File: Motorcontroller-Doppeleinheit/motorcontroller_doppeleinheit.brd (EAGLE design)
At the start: 75 x 65 mm, 24 parts, among them Q1 16,384Mhz

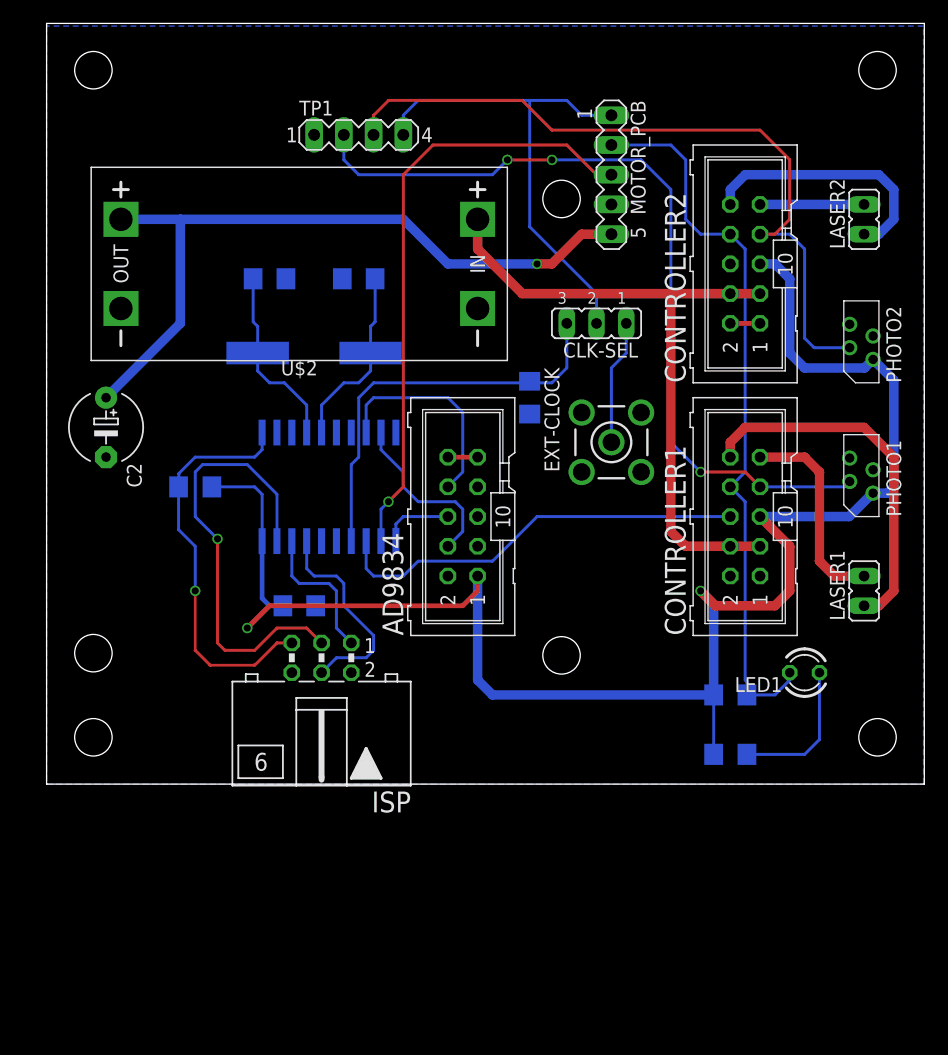
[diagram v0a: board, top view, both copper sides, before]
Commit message: Added R4 for current limit if powering on
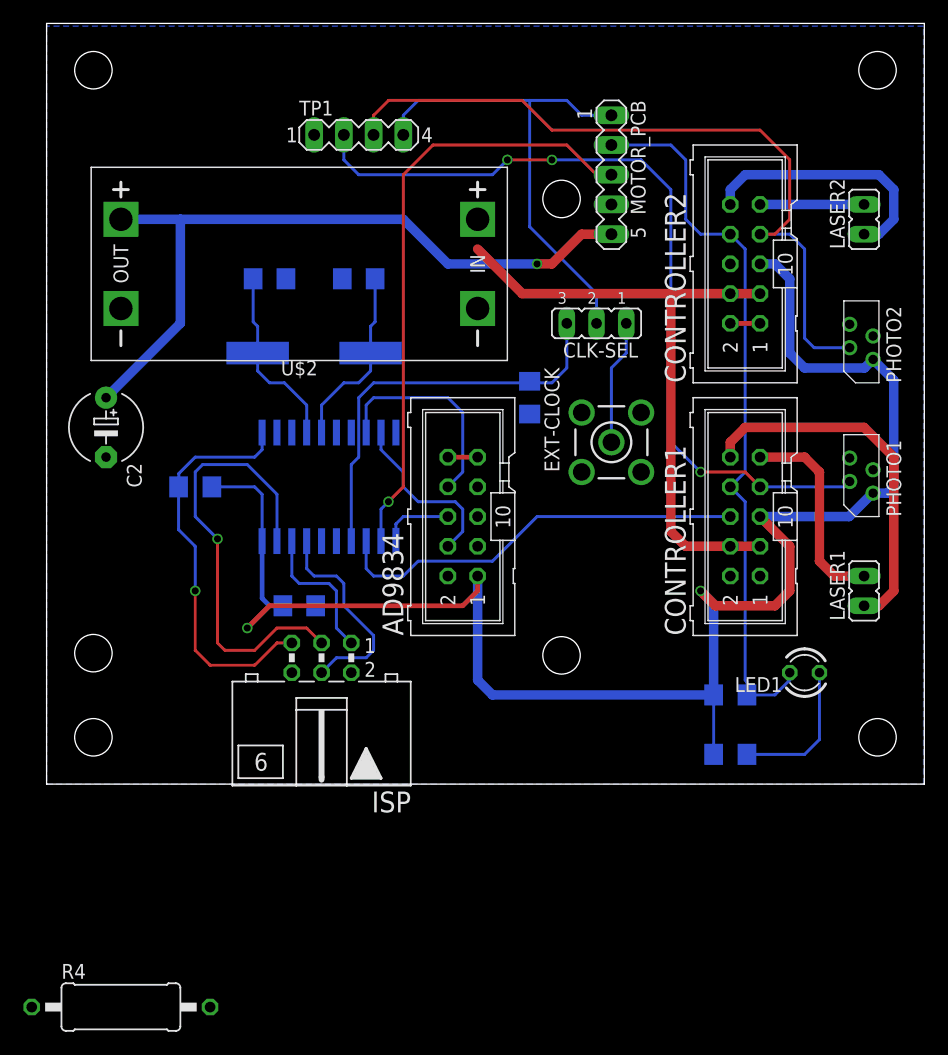
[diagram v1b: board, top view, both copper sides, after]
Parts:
- added R4: 1,2Ohm 1W, rcl:0411/15
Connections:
- new net N$6: R4.1, U$2.IN+
- net +12V: now also R4.2; no longer U$2.IN+
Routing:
- net +12V: track 56.7 -> 54.2 mm
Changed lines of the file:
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@@
 <element name="R3" library="rcl" package="R1206" value="10k" x="58.42" y="7.62" rot="MR0"/>
 <element name="C5" library="rcl" package="C1206" value="1n" x="41.275" y="33.02" rot="MR270"/>
+<element name="R4" library="rcl" package="0411/15" value="1,2Ohm 1W" x="6.35" y="-19.05"/>
 </elements>
 <signals>
@@
 <contactref element="CONTROLLER2" pad="4"/>
 <contactref element="CONTROLLER2" pad="3"/>
-<contactref element="U$2" pad="IN+"/>
 <wire x1="60.96" y1="41.91" x2="58.42" y2="41.91" width="0.8128" layer="1"/>
 <wire x1="58.42" y1="41.91" x2="53.34" y2="41.91" width="0.8128" layer="1"/>
@@
 <wire x1="53.34" y1="21.59" x2="53.34" y2="41.91" width="0.8128" layer="1"/>
 <wire x1="40.64" y1="41.91" x2="36.83" y2="45.72" width="0.8128" layer="1"/>
-<wire x1="36.83" y1="45.72" x2="36.83" y2="48.26" width="0.8128" layer="1"/>
+<contactref element="R4" pad="2"/>
+<wire x1="13.97" y1="-19.05" x2="54.61" y2="20.32" width="0" layer="19" extent="1-1"/>
 </signal>
 <signal name="+24V">
@@
 <wire x1="19.05" y1="34.29" x2="20.32" y2="34.29" width="0.254" layer="16"/>
 </signal>
+<signal name="N$6">
+<contactref element="U$2" pad="IN+"/>
+<contactref element="R4" pad="1"/>
+<wire x1="-1.27" y1="-19.05" x2="36.83" y2="48.26" width="0" layer="19" extent="1-1"/>
+</signal>
 </signals>
